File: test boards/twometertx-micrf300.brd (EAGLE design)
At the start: 13.8 x 21.4 mm, 12 parts

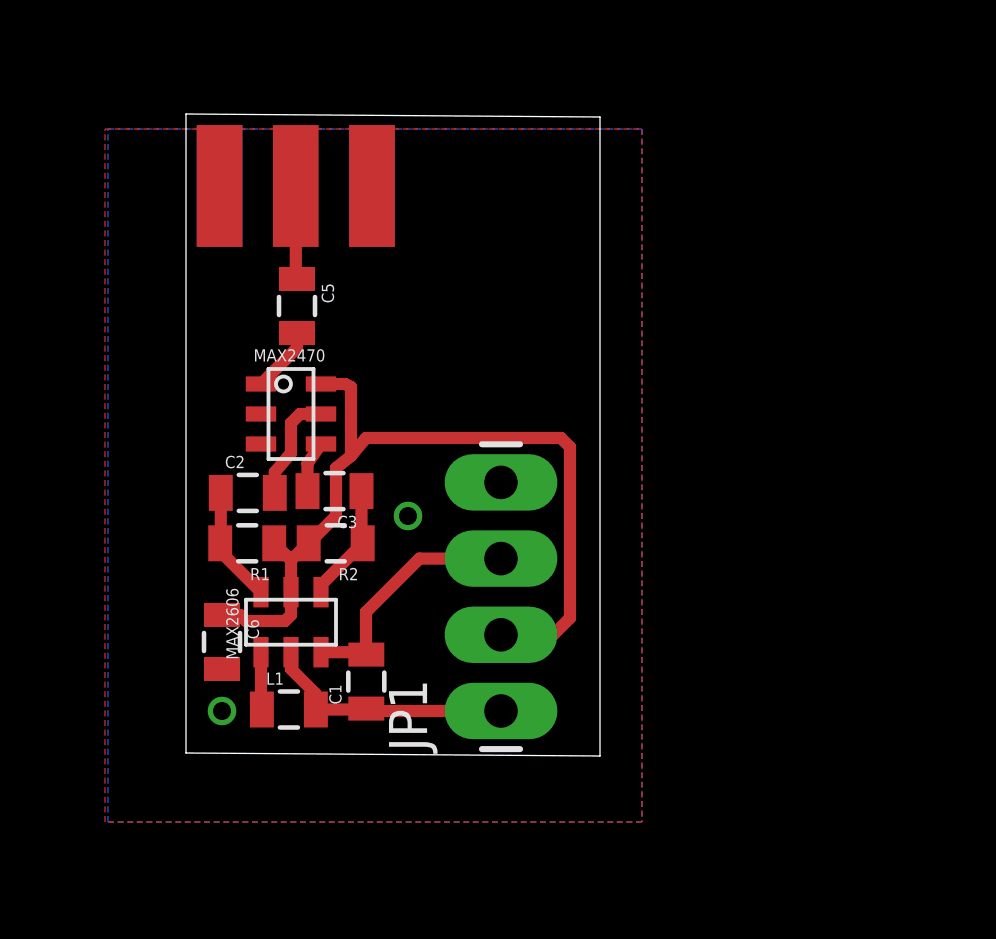
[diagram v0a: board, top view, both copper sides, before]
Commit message: updates
added twometertx-micrf300, changed layout of twometertx, changed led
layout on programmer shield to correct an error, added tracksoar v1.1
to swap power and ground pins on power input header
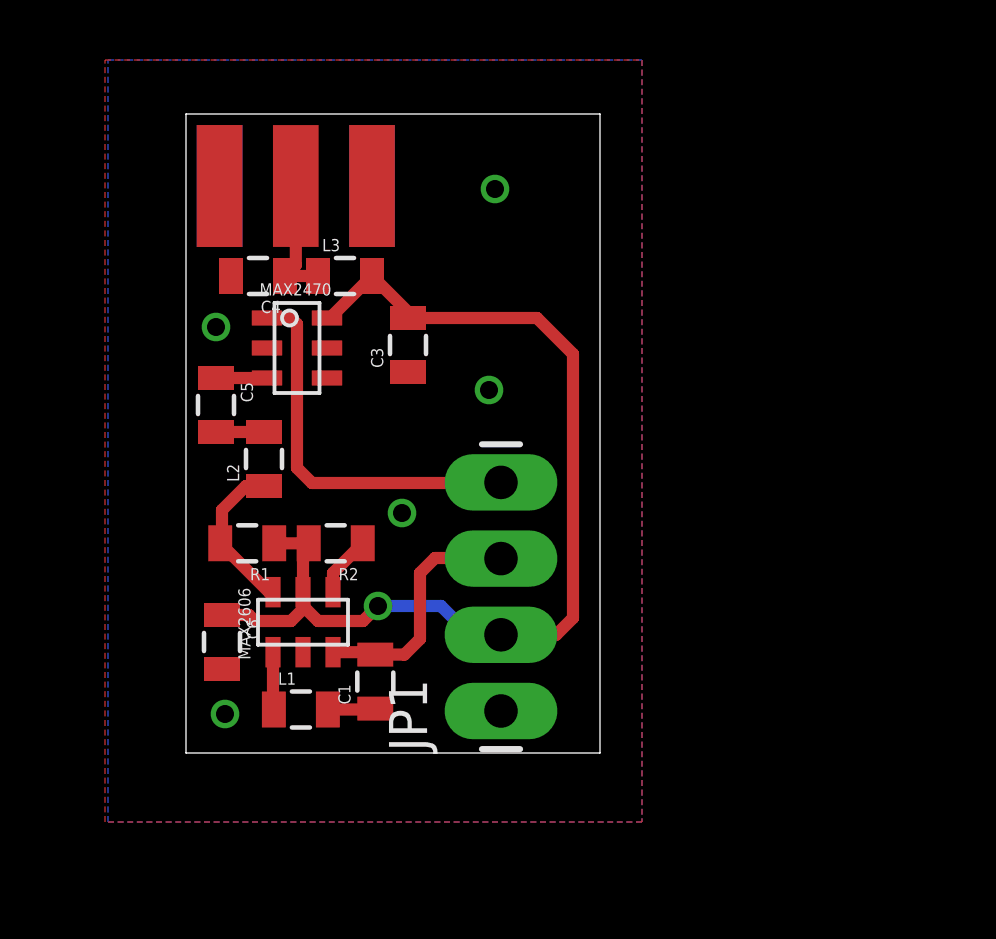
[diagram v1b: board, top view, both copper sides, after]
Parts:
- removed C2: (no value), SparkFun-Capacitors:0805
- added C4: (no value), SparkFun-Capacitors:0805
- added L2, L3: (no value), SparkFun-Passives:0805
- moved C3 5.45 mm to (15.7, 19.1), turned to 90 degrees
- moved C5 4.26 mm to (9.30, 17.1)
- moved U$2 2.21 mm to (12.0, 19.0)
- moved L1 0.40 mm to (12.1, 6.95)
- moved U$1 0.40 mm to (12.2, 9.86)
- moved C1 0.30 mm to (14.6, 7.88)
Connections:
- removed net IN-: C3.2, U$2.P$4
- removed net OUT-: C5.2, U$2.P$1
- removed net THING: C2.1, R1.2, U$1.P$6
- new net EN: JP1.4, U$2.P$1
- new net N$1: C5.1, U$2.P$3
- new net N$4: C5.2, L2.2
- net 5V: now also C3.2, L3.2
- net GND: now also C3.1, C4.2, U$2.P$4, U$2.P$5
- net IN+: now also L2.1, R1.2, U$1.P$6; no longer C2.2, U$2.P$5
- net RFOUT: now also C4.1, L3.1; no longer C5.1
- net THING2: no longer C3.1
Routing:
- net EN: track 0.00 -> 12.9 mm
- net GND: track 8.47 -> 1.59 mm, vias 2 -> 5
- net 5V: track 28.7 -> 35.1 mm, vias 0 -> 1
- net THING: track 3.88 -> 0.00 mm
- net OUT-: track 2.20 -> 0.00 mm
- net THING2: track 3.96 -> 2.04 mm
- net IN-: track 1.71 -> 0.00 mm
- net N$1: track 0.00 -> 1.70 mm
- net IN+: track 3.65 -> 5.30 mm
- net N$4: track 0.00 -> 1.60 mm
- net RFOUT: track 3.12 -> 4.25 mm
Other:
- board size 13.8 x 21.4 mm -> 13.8 x 21.3 mm

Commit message: resolved 1.6.5+ compiling issues
resolved issues in afsk_avr.cpp / h that prevented the firmware from
compiling in 1.6.5+
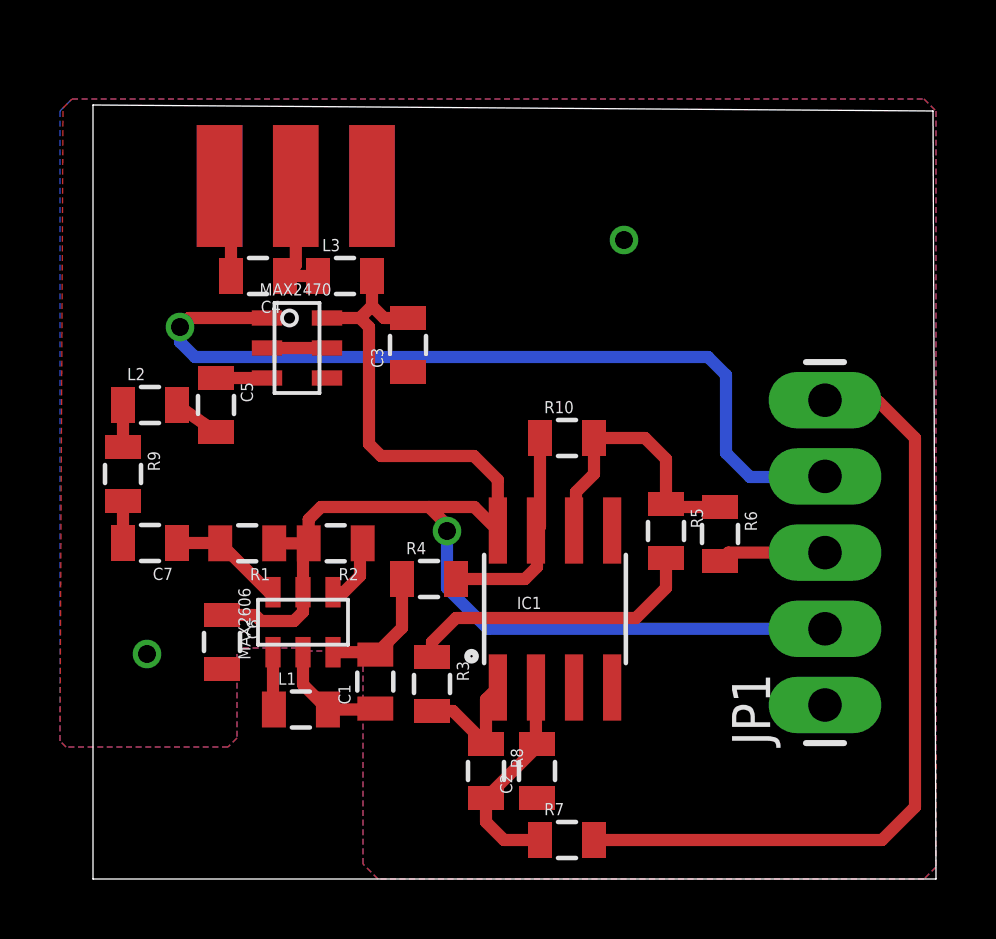
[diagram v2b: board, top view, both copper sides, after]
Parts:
- added C2: (no value), SparkFun-Capacitors:0805
- added C7: 22pf NPO, SparkFun-Capacitors:0805
- added IC1: LMV358SOIC, SparkFun-AnalogIC:SO08
- added R10, R3, R4, R5, R6, R7, R8, R9: (no value), SparkFun-Passives:0805
- JP1: device SparkFun-Connectors:1X04_LONGPADS -> SparkFun-Connectors:1X05_LONGPADS
- moved JP1 10.8 mm to (29.6, 7.10)
- moved L2 4.20 mm to (7.10, 17.1), turned to 0 degrees
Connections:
- new net N$11: IC1.1, R3.2, R8.1
- new net N$3: C2.2, IC1.2, R7.1, R8.2
- new net N$5: R3.1, R5.2
- new net N$6: IC1.7, R10.1, R4.2
- new net N$7: IC1.6, R10.2, R5.1, R6.1
- new net N$8: L2.1, R9.1
- new net N$9: C7.1, R1.2, U$1.P$6
- new net SIG: JP1.3, R6.2
- new net TUNE_OFFSET: JP1.5, R7.2
- net 5V: now also IC1.8
- net GND: now also C2.1, IC1.3, IC1.4, IC1.5
- net IN+: now also C7.2, R9.2; no longer L2.1, R1.2, U$1.P$6
- net TUNE: now also R4.1; no longer JP1.3
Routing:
- net TUNE_OFFSET: track 0.00 -> 27.0 mm
- net EN: track 12.9 -> 28.4 mm, vias 0 -> 1
- net N$5: track 0.00 -> 10.0 mm
- net 5V: track 35.1 -> 45.0 mm
- net N$7: track 0.00 -> 9.39 mm
- net GND: track 1.59 -> 9.00 mm, vias 5 -> 2
- net N$3: track 0.00 -> 7.25 mm
- net N$6: track 0.00 -> 7.24 mm
- net N$11: track 0.00 -> 4.30 mm
- net TUNE: track 8.26 -> 4.33 mm
- net IN+: track 5.30 -> 1.40 mm
- net N$9: track 0.00 -> 3.88 mm
- net SIG: track 0.00 -> 3.62 mm
- net N$8: track 0.00 -> 1.40 mm
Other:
- board size 13.8 x 21.3 mm -> 28.1 x 25.8 mm
